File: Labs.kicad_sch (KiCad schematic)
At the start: 29 parts, among them J1 Conn_02x05_Counter_Clockwise, SW1BOOT1 SW_Push, SW2NRST1 SW_Push, U1 STM32F407VGTx, Y1 Crystal

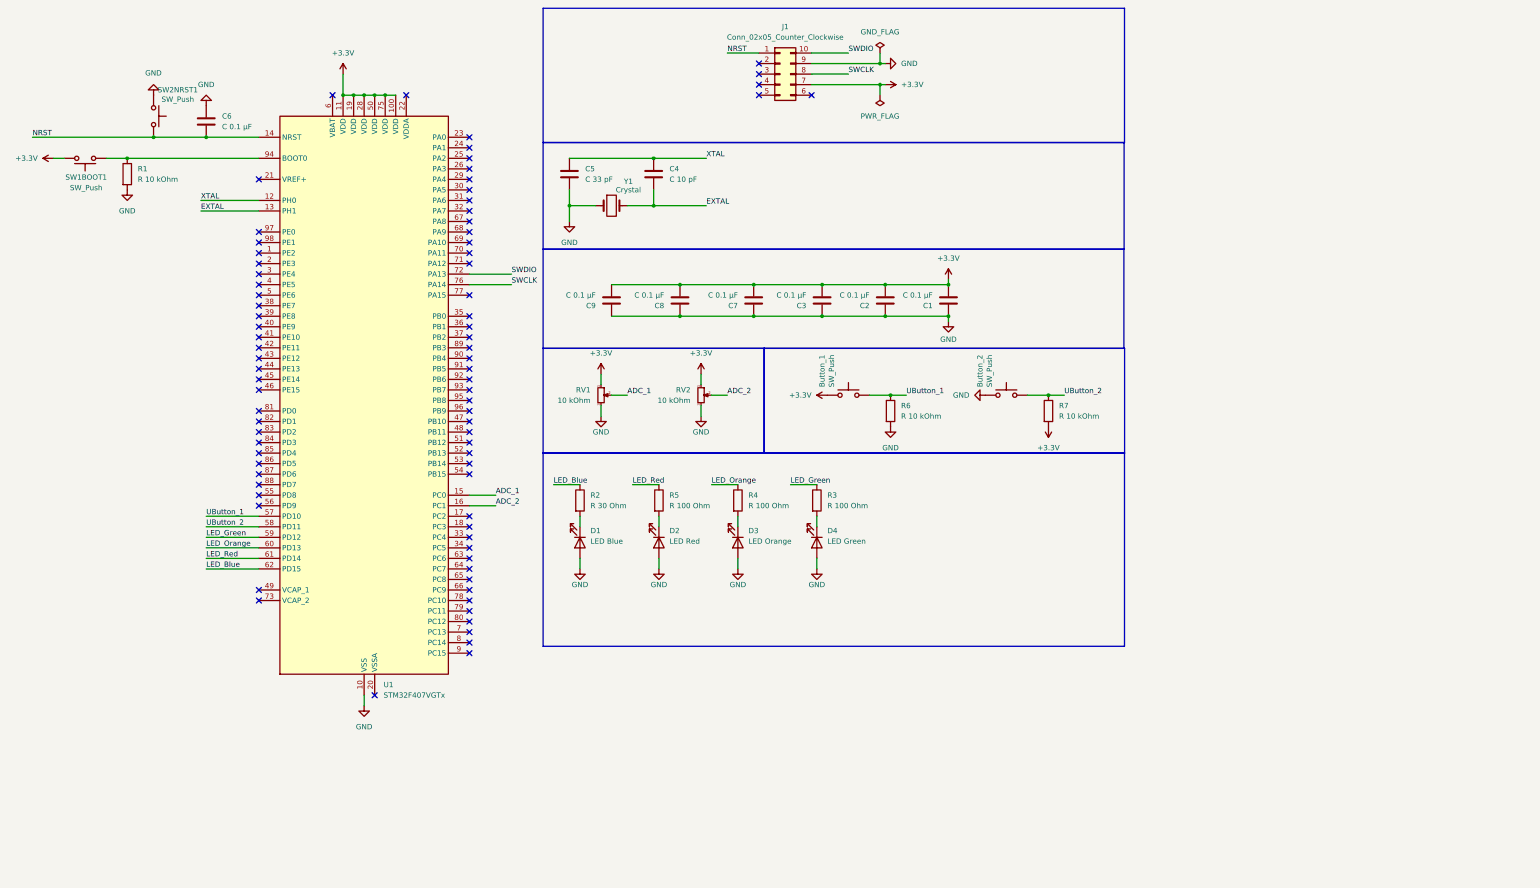
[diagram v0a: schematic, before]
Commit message: feat: add communication interfaces
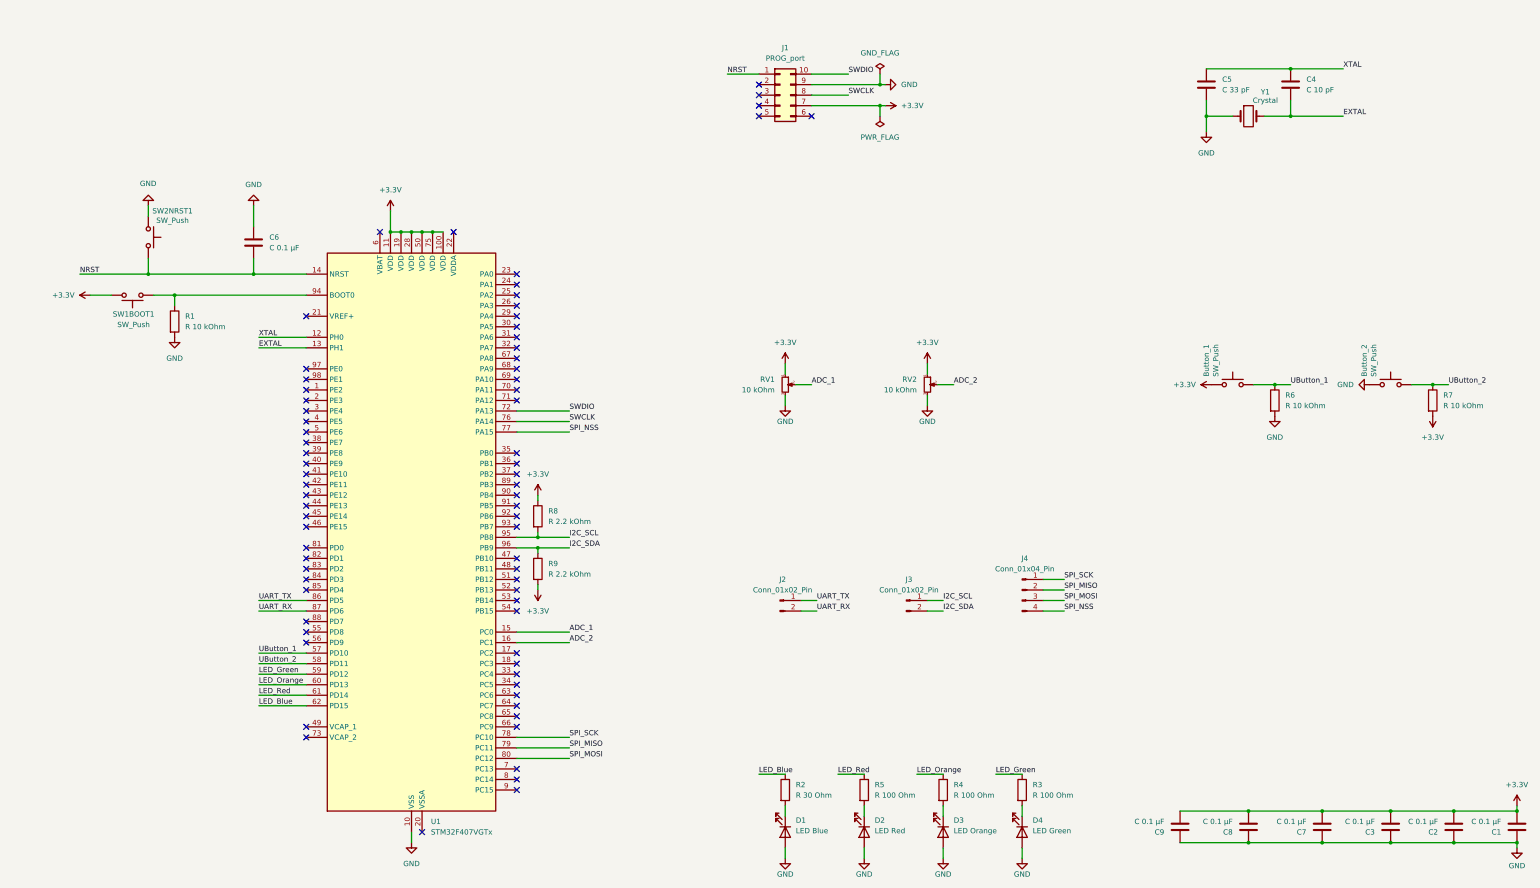
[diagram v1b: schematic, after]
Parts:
- added J2, J3: Conn_01x02_Pin, Connector_PinHeader_1.00mm:PinHeader_1x02_P1.00mm_Horizontal, symbol Connector:Conn_01x02_Pin
- added J4: Conn_01x04_Pin, Connector_PinHeader_1.00mm:PinHeader_1x04_P1.00mm_Horizontal, symbol Connector:Conn_01x04_Pin
- added R8, R9: R 2.2 kOhm, Resistor_SMD:R_0805_2012Metric_Pad1.20x1.40mm_HandSolder, symbol Device:R
- J1: value Conn_02x05_Counter_Clockwise -> PROG_port
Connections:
- net +3.3V: now also R8.1, R9.2
- net SPI_NSS: now reaches U1.77 (PA15)
- net SPI_NSS: now also J4.4 (Pin_4)
- net SPI_SCK: now reaches U1.78 (PC10)
- net SPI_SCK: now also J4.1 (Pin_1)
- net SPI_MISO: now reaches U1.79 (PC11)
- net SPI_MISO: now also J4.2 (Pin_2)
- net SPI_MOSI: now reaches U1.80 (PC12)
- net SPI_MOSI: now also J4.3 (Pin_3)
- net UART_TX: now reaches U1.86 (PD5)
- net UART_TX: now also J2.1 (Pin_1)
- net UART_RX: now reaches U1.87 (PD6)
- net UART_RX: now also J2.2 (Pin_2)
- net I2C_SCL: now reaches U1.95 (PB8)
- net I2C_SCL: now also J3.1 (Pin_1), R8.2
- net I2C_SDA: now reaches U1.96 (PB9)
- net I2C_SDA: now also J3.2 (Pin_2), R9.1
- no-connect marks 81 -> 73
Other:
- moved on the sheet: Button_1, Button_2, C1, C2, C3, C4, C5, C6, C7, C8, C9, D1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

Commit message: feat: add tracing
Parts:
- J2, J3: footprint Connector_PinHeader_1.00mm:PinHeader_1x02_P1.00mm_Horizontal -> Connector_PinHeader_2.54mm:PinHeader_1x02_P2.54mm_Horizontal
- J4: footprint Connector_PinHeader_1.00mm:PinHeader_1x04_P1.00mm_Horizontal -> Connector_PinHeader_2.54mm:PinHeader_1x04_P2.54mm_Horizontal
- RV1, RV2: footprint Potentiometer_THT:Potentiometer_ACP_CA9-V10_Vertical -> Potentiometer_THT:Potentiometer_Bourns_3266Y_Vertical
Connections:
- net +3.3V: now also R9.1; no longer R9.2
- net I2C_SCL: now also J3.2 (Pin_2); no longer J3.1 (Pin_1)
- net I2C_SDA: now also J3.1 (Pin_1), R9.2; no longer J3.2 (Pin_2), R9.1
- net SPI_MOSI: now also J4.1 (Pin_1); no longer J4.3 (Pin_3)
- net SPI_SCK: now also J4.3 (Pin_3); no longer J4.1 (Pin_1)
- net UART_RX: now also J2.1 (Pin_1); no longer J2.2 (Pin_2)
- net UART_TX: now also J2.2 (Pin_2); no longer J2.1 (Pin_1)
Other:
- moved on the sheet: J2, R9
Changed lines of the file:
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@@
 	(wire
 		(pts
+			(xy 209.55 154.94) (xy 213.36 154.94)
+		)
+		(stroke
+			(width 0)
+			(type default)
+		)
+	)
+	(wire
+		(pts
 			(xy 215.9 196.85) (xy 222.25 196.85)
 		)
@@
 	(wire
 		(pts
-			(xy 138.43 114.3) (xy 151.13 114.3)
+			(xy 265.43 149.86) (xy 270.51 149.86)
 		)
 		(stroke
@@
 	(wire
 		(pts
-			(xy 209.55 33.02) (xy 218.44 33.02)
+			(xy 138.43 114.3) (xy 151.13 114.3)
 		)
 		(stroke
@@
 	(wire
 		(pts
-			(xy 55.88 81.28) (xy 87.63 81.28)
+			(xy 209.55 33.02) (xy 218.44 33.02)
 		)
 		(stroke
@@
 	(wire
 		(pts
-			(xy 138.43 142.24) (xy 143.51 142.24)
+			(xy 55.88 81.28) (xy 87.63 81.28)
 		)
 		(stroke
@@
 	(wire
 		(pts
-			(xy 222.25 214.63) (xy 222.25 217.17)
+			(xy 138.43 142.24) (xy 143.51 142.24)
 		)
 		(stroke
@@
 	(wire
 		(pts
-			(xy 314.96 205.74) (xy 298.45 205.74)
+			(xy 222.25 214.63) (xy 222.25 217.17)
 		)
 		(stroke
@@
 	(wire
 		(pts
-			(xy 138.43 139.7) (xy 143.51 139.7)
+			(xy 314.96 205.74) (xy 298.45 205.74)
 		)
 		(stroke
@@
 	(wire
 		(pts
-			(xy 265.43 149.86) (xy 270.51 149.86)
+			(xy 138.43 139.7) (xy 143.51 139.7)
 		)
 		(stroke
@@
 	(wire
 		(pts
-			(xy 237.49 105.41) (xy 237.49 107.95)
+			(xy 209.55 157.48) (xy 213.36 157.48)
 		)
 		(stroke
@@
 	(wire
 		(pts
-			(xy 203.2 97.79) (xy 203.2 100.33)
+			(xy 237.49 105.41) (xy 237.49 107.95)
 		)
 		(stroke
@@
 	(wire
 		(pts
-			(xy 118.11 66.04) (xy 120.65 66.04)
+			(xy 203.2 97.79) (xy 203.2 100.33)
 		)
 		(stroke
@@
 	(wire
 		(pts
-			(xy 226.06 35.56) (xy 227.33 35.56)
+			(xy 118.11 66.04) (xy 120.65 66.04)
 		)
 		(stroke
@@
 	(wire
 		(pts
-			(xy 260.35 214.63) (xy 260.35 217.17)
+			(xy 226.06 35.56) (xy 227.33 35.56)
 		)
 		(stroke
@@
 	(wire
 		(pts
-			(xy 76.2 170.18) (xy 87.63 170.18)
+			(xy 260.35 214.63) (xy 260.35 217.17)
 		)
 		(stroke
@@
 	(wire
 		(pts
-			(xy 316.23 102.87) (xy 321.31 102.87)
+			(xy 76.2 170.18) (xy 87.63 170.18)
 		)
 		(stroke
@@
 	(wire
 		(pts
-			(xy 237.49 157.48) (xy 241.3 157.48)
+			(xy 316.23 102.87) (xy 321.31 102.87)
 		)
 		(stroke
@@
 	(wire
 		(pts
-			(xy 265.43 154.94) (xy 270.51 154.94)
-		)
-		(stroke
-			(width 0)
-			(type default)
-		)
-	)
-	(wire
-		(pts
 			(xy 74.93 59.69) (xy 74.93 64.77)
 		)
@@
 	(wire
 		(pts
-			(xy 237.49 154.94) (xy 241.3 154.94)
-		)
-		(stroke
-			(width 0)
-			(type default)
-		)
-	)
-	(wire
-		(pts
 			(xy 203.2 214.63) (xy 203.2 217.17)
 		)
@@
 	(wire
 		(pts
+			(xy 265.43 154.94) (xy 270.51 154.94)
+		)
+		(stroke
+			(width 0)
+			(type default)
+		)
+	)
+	(wire
+		(pts
 			(xy 209.55 27.94) (xy 218.44 27.94)
 		)
@@
 	(wire
 		(pts
+			(xy 237.49 157.48) (xy 241.3 157.48)
+		)
+		(stroke
+			(width 0)
+			(type default)
+		)
+	)
+	(wire
+		(pts
 			(xy 138.43 193.04) (xy 151.13 193.04)
 		)
@@
 	(wire
 		(pts
-			(xy 379.73 204.47) (xy 379.73 205.74)
+			(xy 237.49 154.94) (xy 241.3 154.94)
 		)
 		(stroke
@@
 	(wire
 		(pts
-			(xy 207.01 157.48) (xy 210.82 157.48)
+			(xy 379.73 204.47) (xy 379.73 205.74)
 		)
 		(stroke
@@
 	(wire
 		(pts
-			(xy 207.01 154.94) (xy 210.82 154.94)
-		)
-		(stroke
-			(width 0)
-			(type default)
-		)
-	)
-	(wire
-		(pts
 			(xy 35.56 81.28) (xy 40.64 81.28)
 		)
@@
 	)
 	(label "I2C_SCL"
-		(at 241.3 154.94 0)
+		(at 241.3 157.48 0)
 		(effects
 			(font
@@
 	)
 	(label "SPI_MOSI"
-		(at 270.51 154.94 0)
+		(at 270.51 149.86 0)
 		(effects
 			(font
@@
 	)
 	(label "I2C_SDA"
-		(at 241.3 157.48 0)
+		(at 241.3 154.94 0)
 		(effects
 			(font
@@
 	)
 	(label "SPI_SCK"
-		(at 270.51 149.86 0)
+		(at 270.51 154.94 0)
 		(effects
 			(font
@@
 	)
 	(label "UART_RX"
-		(at 210.82 157.48 0)
+		(at 213.36 154.94 0)
 		(effects
 			(font
@@
 	)
 	(label "UART_TX"
-		(at 210.82 154.94 0)
+		(at 213.36 157.48 0)
 		(effects
 			(font
@@
 	(symbol
 		(lib_id "Connector:Conn_01x02_Pin")
-		(at 201.93 154.94 0)
+		(at 204.47 154.94 0)
 		(unit 1)
 		(exclude_from_sim no)
@@
 		(fields_autoplaced yes)
 		(property "Reference" "J2"
-			(at 202.565 149.86 0)
+			(at 205.105 149.86 0)
 			(effects
 				(font
@@
 		)
 		(property "Value" "Conn_01x02_Pin"
-			(at 202.565 152.4 0)
+			(at 205.105 152.4 0)
 			(effects
 				(font
@@
 			)
 		)
-		(property "Footprint" "Connector_PinHeader_1.00mm:PinHeader_1x02_P1.00mm_Horizontal"
-			(at 201.93 154.94 0)
+		(property "Footprint" "Connector_PinHeader_2.54mm:PinHeader_1x02_P2.54mm_Horizontal"
+			(at 204.47 154.94 0)
 			(effects
 				(font
@@
 		)
 		(property "Datasheet" "~"
-			(at 201.93 154.94 0)
+			(at 204.47 154.94 0)
 			(effects
 				(font
@@
 		)
 		(property "Description" "Generic connector, single row, 01x02, script generated"
-			(at 201.93 154.94 0)
+			(at 204.47 154.94 0)
 			(effects
 				(font
@@
 			)
 		)
-		(property "Footprint" "Connector_PinHeader_1.00mm:PinHeader_1x02_P1.00mm_Horizontal"
+		(property "Footprint" "Connector_PinHeader_2.54mm:PinHeader_1x02_P2.54mm_Horizontal"
 			(at 232.41 154.94 0)
 			(effects
@@
 	(symbol
 		(lib_id "Device:R")
-		(at 143.51 147.32 0)
+		(at 143.51 147.32 180)
 		(unit 1)
 		(exclude_from_sim no)
@@
 					(size 1.27 1.27)
 				)
-				(justify left)
+				(justify right)
 			)
 		)
@@
 					(size 1.27 1.27)
 				)
-				(justify left)
+				(justify right)
 			)
 		)
 		(property "Footprint" "Resistor_SMD:R_0805_2012Metric_Pad1.20x1.40mm_HandSolder"
-			(at 141.732 147.32 90)
+			(at 145.288 147.32 90)
 			(effects
 				(font
@@
 			)
 		)
-		(property "Footprint" "Potentiometer_THT:Potentiometer_ACP_CA9-V10_Vertical"
+		(property "Footprint" "Potentiometer_THT:Potentiometer_Bourns_3266Y_Vertical"
 			(at 203.2 102.87 0)
 			(effects
@@
 			)
 		)
-		(property "Footprint" "Potentiometer_THT:Potentiometer_ACP_CA9-V10_Vertical"
+		(property "Footprint" "Potentiometer_THT:Potentiometer_Bourns_3266Y_Vertical"
 			(at 237.49 102.87 0)
 			(effects
@@
 			)
 		)
-		(property "Footprint" "Connector_PinHeader_1.00mm:PinHeader_1x04_P1.00mm_Horizontal"
+		(property "Footprint" "Connector_PinHeader_2.54mm:PinHeader_1x04_P2.54mm_Horizontal"
 			(at 260.35 152.4 0)
 			(effects

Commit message: fix: minor fixes
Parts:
- removed J2, J3: Conn_01x02_Pin, Connector_PinHeader_2.54mm:PinHeader_1x02_P2.54mm_Horizontal, symbol Connector:Conn_01x02_Pin
- added J2: Conn_01x03_Pin, Connector_PinSocket_2.54mm:PinSocket_1x03_P2.54mm_Horizontal, symbol Connector:Conn_01x03_Pin
- added J3: Conn_01x04_Pin, Connector_PinHeader_2.54mm:PinHeader_1x04_P2.54mm_Horizontal, symbol Connector:Conn_01x04_Pin
- renumbered C6 to C1, C9 to C2, C5 to C3, C8 to C4, C4 to C5, C7 to C6, C3 to C7, C2 to C8, C1 to C9, R8 to R2, R9 to R3, R2 to R4, R4 to R6, R3 to R7, R6 to R8, R7 to R9
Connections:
- net +3.3V: now also J3.1 (Pin_1)
- net GND: now also J2.3 (Pin_3), J3.4 (Pin_4)
- net I2C_SCL: now also J3.3 (Pin_3)
- net I2C_SDA: now also J3.2 (Pin_2)
- net UART_RX: now also J2.1 (Pin_1)
- net UART_TX: now also J2.2 (Pin_2)

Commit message: fix: minor fixes
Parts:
- J2: footprint Connector_PinSocket_2.54mm:PinSocket_1x03_P2.54mm_Horizontal -> Connector_PinHeader_2.54mm:PinHeader_1x03_P2.54mm_Horizontal
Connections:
- net GND: now also J2.1 (Pin_1); no longer J2.3 (Pin_3)
- net UART_RX: now also J2.2 (Pin_2); no longer J2.1 (Pin_1)
- net UART_TX: now also J2.3 (Pin_3); no longer J2.2 (Pin_2)
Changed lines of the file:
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@@
 	(wire
 		(pts
-			(xy 209.55 152.4) (xy 213.36 152.4)
+			(xy 215.9 196.85) (xy 222.25 196.85)
 		)
 		(stroke
@@
 	(wire
 		(pts
-			(xy 215.9 196.85) (xy 222.25 196.85)
+			(xy 364.49 213.36) (xy 349.25 213.36)
 		)
 		(stroke
@@
 	(wire
 		(pts
-			(xy 364.49 213.36) (xy 349.25 213.36)
+			(xy 209.55 154.94) (xy 213.36 154.94)
 		)
 		(stroke
@@
 	(wire
 		(pts
-			(xy 143.51 143.51) (xy 143.51 142.24)
+			(xy 209.55 157.48) (xy 213.36 157.48)
 		)
 		(stroke
@@
 	(wire
 		(pts
-			(xy 196.85 196.85) (xy 203.2 196.85)
+			(xy 143.51 143.51) (xy 143.51 142.24)
 		)
 		(stroke
@@
 	(wire
 		(pts
-			(xy 209.55 154.94) (xy 213.36 154.94)
+			(xy 196.85 196.85) (xy 203.2 196.85)
 		)
 		(stroke
@@
 	(wire
 		(pts
-			(xy 213.36 157.48) (xy 209.55 157.48)
+			(xy 74.93 59.69) (xy 74.93 64.77)
 		)
 		(stroke
@@
 	(wire
 		(pts
-			(xy 74.93 59.69) (xy 74.93 64.77)
+			(xy 76.2 154.94) (xy 87.63 154.94)
 		)
 		(stroke
@@
 	(wire
 		(pts
-			(xy 76.2 154.94) (xy 87.63 154.94)
+			(xy 49.53 72.39) (xy 49.53 76.2)
 		)
 		(stroke
@@
 	(wire
 		(pts
-			(xy 49.53 72.39) (xy 49.53 76.2)
+			(xy 55.88 81.28) (xy 50.8 81.28)
 		)
 		(stroke
@@
 	(wire
 		(pts
-			(xy 55.88 81.28) (xy 50.8 81.28)
+			(xy 107.95 66.04) (xy 110.49 66.04)
 		)
 		(stroke
@@
 	(wire
 		(pts
-			(xy 107.95 66.04) (xy 110.49 66.04)
+			(xy 254 196.85) (xy 260.35 196.85)
 		)
 		(stroke
@@
 	(wire
 		(pts
-			(xy 254 196.85) (xy 260.35 196.85)
+			(xy 349.25 205.74) (xy 332.74 205.74)
 		)
 		(stroke
@@
 	(wire
 		(pts
-			(xy 349.25 205.74) (xy 332.74 205.74)
+			(xy 209.55 152.4) (xy 214.63 152.4)
 		)
 		(stroke
@@
 	(wire
 		(pts
-			(xy 213.36 158.75) (xy 213.36 157.48)
-		)
-		(stroke
-			(width 0)
-			(type default)
-		)
-	)
-	(wire
-		(pts
 			(xy 359.41 102.87) (xy 363.22 102.87)
 		)
@@
 	)
 	(label "UART_RX"
-		(at 213.36 152.4 0)
+		(at 213.36 154.94 0)
 		(effects
 			(font
@@
 	)
 	(label "UART_TX"
-		(at 213.36 154.94 0)
+		(at 213.36 157.48 0)
 		(effects
 			(font
@@
 	(symbol
 		(lib_id "power:GND")
-		(at 213.36 158.75 0)
+		(at 214.63 152.4 180)
 		(unit 1)
 		(exclude_from_sim no)
@@
 		(fields_autoplaced yes)
 		(property "Reference" "#PWR012"
-			(at 213.36 165.1 0)
+			(at 214.63 146.05 0)
 			(effects
 				(font
@@
 		)
 		(property "Value" "GND"
-			(at 213.36 163.83 0)
+			(at 214.63 147.32 0)
 			(effects
 				(font
@@
 		)
 		(property "Footprint" ""
-			(at 213.36 158.75 0)
+			(at 214.63 152.4 0)
 			(effects
 				(font
@@
 		)
 		(property "Datasheet" ""
-			(at 213.36 158.75 0)
+			(at 214.63 152.4 0)
 			(effects
 				(font
@@
 		)
 		(property "Description" "Power symbol creates a global label with name \"GND\" , ground"
-			(at 213.36 158.75 0)
+			(at 214.63 152.4 0)
 			(effects
 				(font
@@
 			)
 		)
-		(property "Footprint" "Connector_PinSocket_2.54mm:PinSocket_1x03_P2.54mm_Horizontal"
+		(property "Footprint" "Connector_PinHeader_2.54mm:PinHeader_1x03_P2.54mm_Horizontal"
 			(at 204.47 154.94 0)
 			(effects

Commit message: fix: minor fixes
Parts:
- renumbered J3 to I2C1, J4 to SPI1, J2 to UART1
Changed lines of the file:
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@@
 		(dnp no)
 		(fields_autoplaced yes)
-		(property "Reference" "J2"
+		(property "Reference" "UART1"
 			(at 205.105 147.32 0)
 			(effects
@@
 			(project ""
 				(path "/5b477a71-f590-4cf6-b140-b4be217c683d"
-					(reference "J2")
+					(reference "UART1")
 					(unit 1)
 				)
@@
 		(on_board yes)
 		(dnp no)
-		(property "Reference" "J3"
+		(property "Reference" "I2C1"
 			(at 236.728 144.78 0)
 			(effects
@@
 			(project "Labs"
 				(path "/5b477a71-f590-4cf6-b140-b4be217c683d"
-					(reference "J3")
+					(reference "I2C1")
 					(unit 1)
 				)
@@
 		(on_board yes)
 		(dnp no)
-		(property "Reference" "J4"
+		(property "Reference" "SPI1"
 			(at 260.985 144.78 0)
 			(effects
@@
 			(project ""
 				(path "/5b477a71-f590-4cf6-b140-b4be217c683d"
-					(reference "J4")
-					(unit 1)
-				)
+					(reference "SPI1")
+					(unit 1)
+				)
